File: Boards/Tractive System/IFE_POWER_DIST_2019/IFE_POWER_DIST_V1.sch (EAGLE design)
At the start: 27 parts, among them X1 5566-8, X2 5566-6

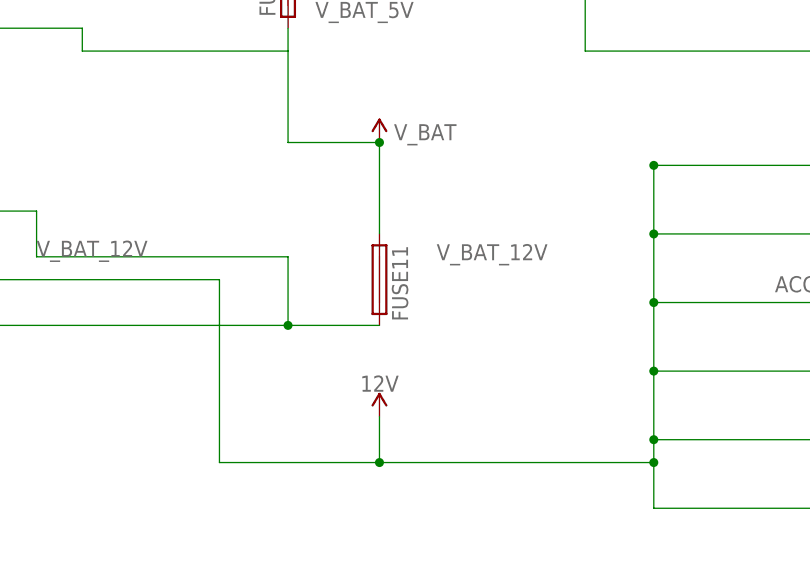
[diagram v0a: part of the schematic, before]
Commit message: fuse replacement
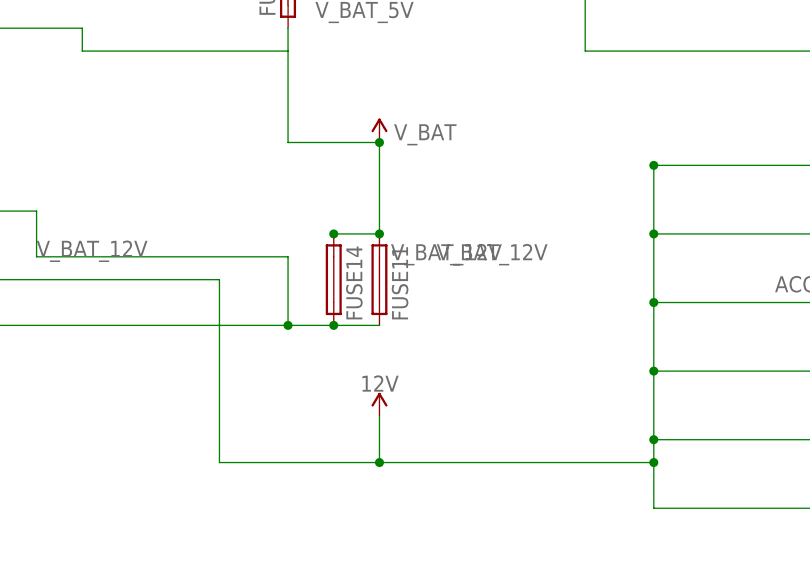
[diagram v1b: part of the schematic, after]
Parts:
- added FUSE14: V_BAT_12V, Fuse:MINI297-3568
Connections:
- net VCC: now also FUSE14.1
- net V_BAT_12V: now also FUSE14.2
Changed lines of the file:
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@@
 <part name="FUSE13" library="Fuse" deviceset="MINI297-3568" device="" value="ACCUMLATOR_5V_5A"/>
 <part name="U$6" library="Display_Custom" deviceset="MINIFIT_JR_5566-02" device=""/>
+<part name="FUSE14" library="Fuse" deviceset="MINI297-3568" device="" value="V_BAT_12V"/>
 </parts>
 <sheets>
@@
 <attribute name="NAME" x="62.23" y="71.755" size="1.778" layer="95"/>
 <attribute name="VALUE" x="62.23" y="63.5" size="1.778" layer="96"/>
+</instance>
+<instance part="FUSE14" gate="G$1" x="-27.94" y="7.62" smashed="yes" rot="R270">
+<attribute name="NAME" x="-26.543" y="11.43" size="1.778" layer="95" rot="R270"/>
+<attribute name="VALUE" x="-21.59" y="9.779" size="1.778" layer="96"/>
 </instance>
 </instances>
@@
 <wire x1="-68.58" y1="38.1" x2="-68.58" y2="35.56" width="0.1524" layer="91"/>
 <junction x="-68.58" y="38.1"/>
+<pinref part="FUSE14" gate="G$1" pin="1"/>
+<wire x1="-22.86" y1="12.7" x2="-27.94" y2="12.7" width="0.1524" layer="91"/>
+<junction x="-22.86" y="12.7"/>
+<junction x="-27.94" y="12.7"/>
 </segment>
 </net>
@@
 <wire x1="-33.02" y1="10.16" x2="-33.02" y2="2.54" width="0.1524" layer="91"/>
 <pinref part="FUSE11" gate="G$1" pin="2"/>
-<wire x1="-33.02" y1="2.54" x2="-22.86" y2="2.54" width="0.1524" layer="91"/>
+<wire x1="-33.02" y1="2.54" x2="-27.94" y2="2.54" width="0.1524" layer="91"/>
 <label x="-60.96" y="10.16" size="1.778" layer="95"/>
+<wire x1="-27.94" y1="2.54" x2="-22.86" y2="2.54" width="0.1524" layer="91"/>
 <wire x1="-33.02" y1="10.16" x2="-60.96" y2="10.16" width="0.1524" layer="91"/>
 <wire x1="-60.96" y1="10.16" x2="-60.96" y2="15.24" width="0.1524" layer="91"/>
@@
 <wire x1="-68.58" y1="5.08" x2="-68.58" y2="2.54" width="0.1524" layer="91"/>
 <junction x="-68.58" y="2.54"/>
-</segment>
-</net>
+<pinref part="FUSE14" gate="G$1" pin="2"/>
+<junction x="-27.94" y="2.54"/>
+</segment>
+</net>
